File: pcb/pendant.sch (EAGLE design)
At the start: 45 parts, among them CON1 USB_MICROSMT+THRUHULE, Q2 16MHz, SW2 BUTTON_2, T1 SSM3J328R,LF, T2 SSM3J328R,LF, U2 MK20D--VFM5, U3 74LVC1G17DCK, U4 74LVC1G17DCK

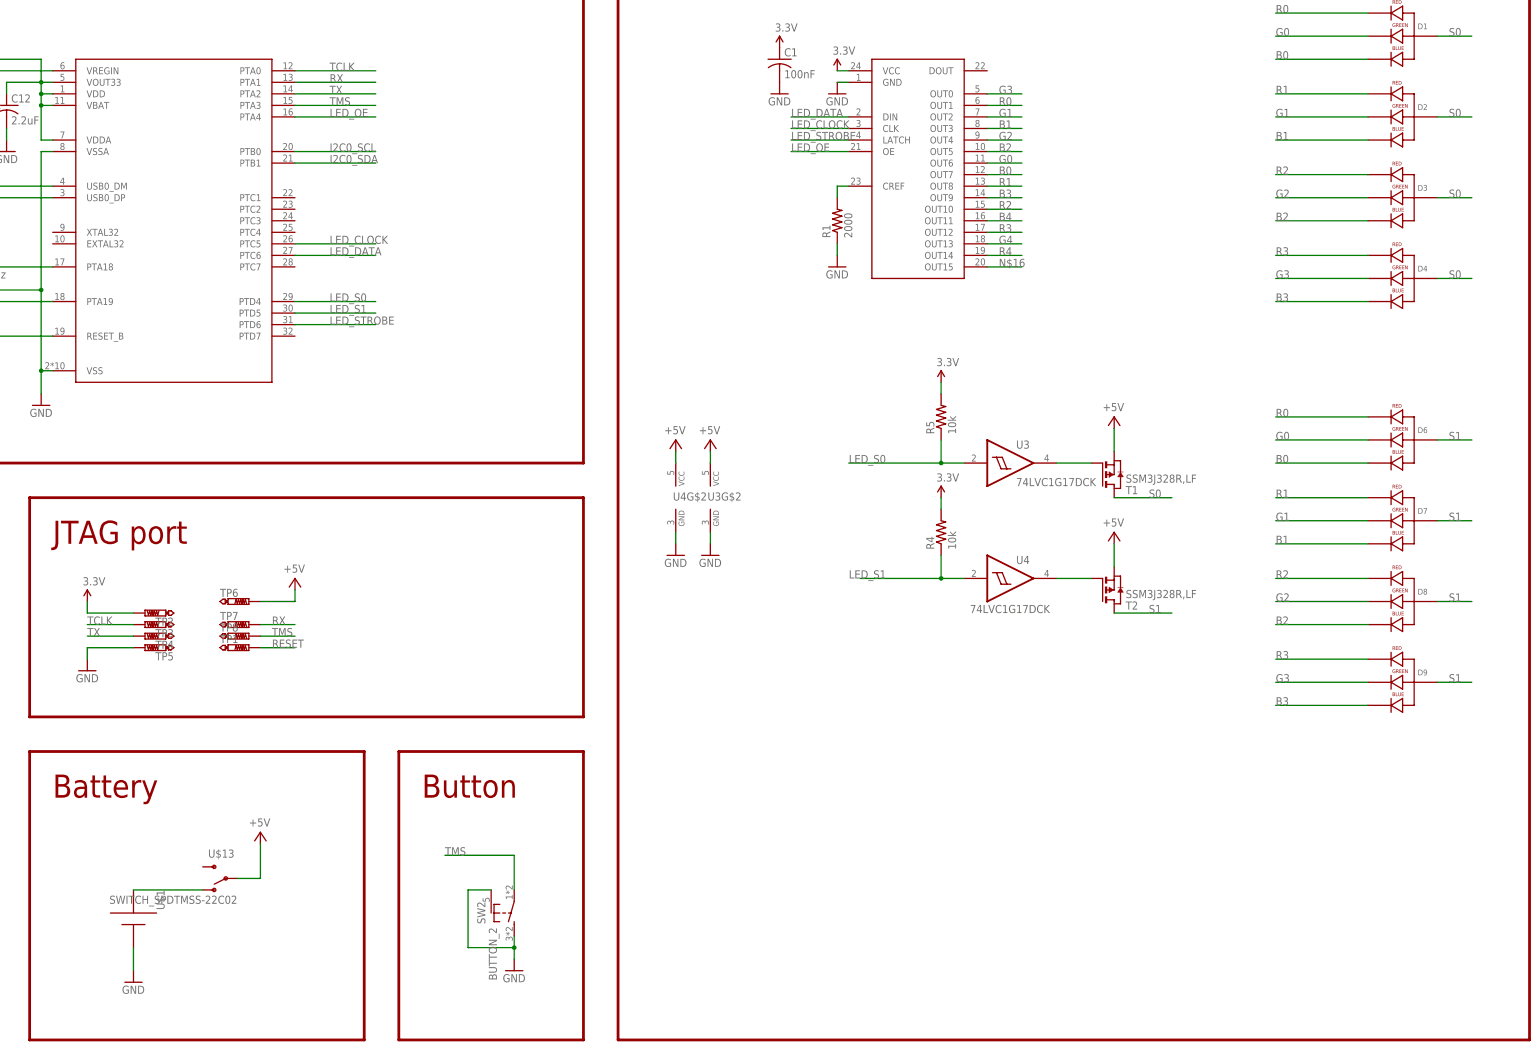
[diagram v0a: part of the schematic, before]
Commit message: fix cap under ICN2026, change led output order, use 5050 LEDs, replace power and tach switches, use 10 LEDs, move test points out from battery
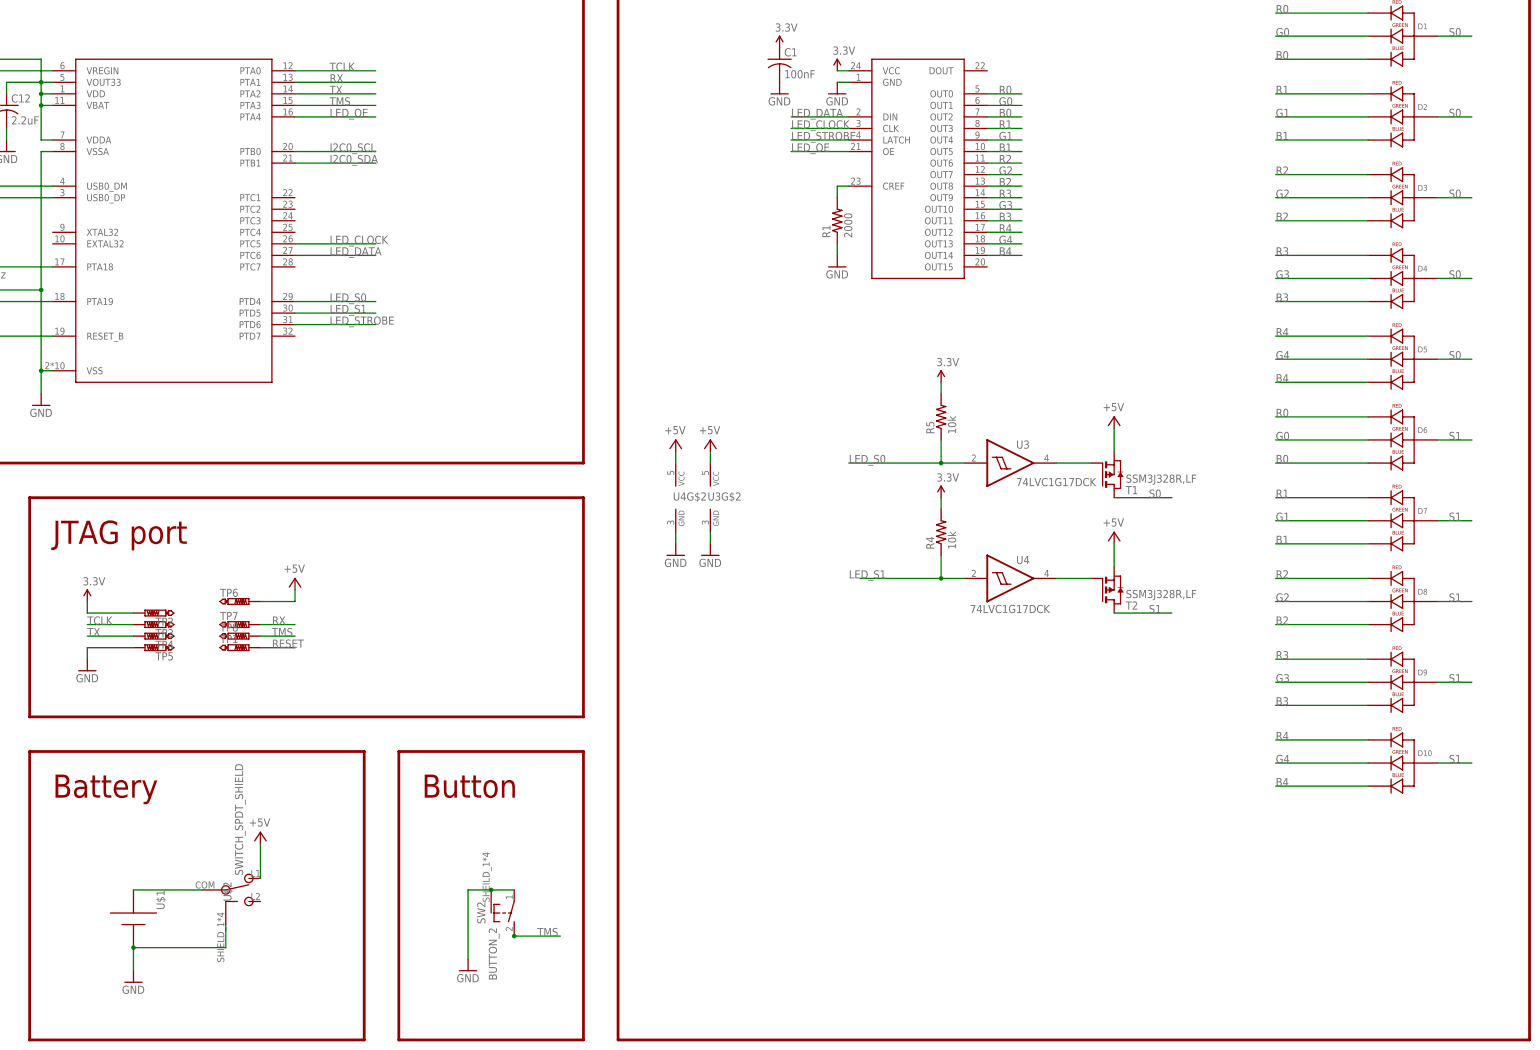
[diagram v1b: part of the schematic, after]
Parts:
- removed U$13: SWITCH_SPDTMSS-22C02, LeoBlinky2014:SWITCH_SPDTMSS-22C02
- added D10, D5: LED-RGB5050, blinkinlabs:LED-RGB5050
- added U$2: SWITCH_SPDT_SHIELD, blinkinlabs:SWITCH_SPDT_SHIELD
- D1, D2, D3, D4, D6, D7, D8, D9: value LED-RGB-CA-THRUCLEAR -> LED-RGB5050; device SparkFun-LED:LED-RGB-CA-THRUCLEAR -> blinkinlabs:LED-RGB5050
- Q2: device blinkinlabs:CRYSTAL_4PAD2520 -> blinkinlabs:CRYSTAL_4PAD
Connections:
- removed net N$16: U$5.OUT15
- net +5V: now also U$2.L1; no longer U$13.P
- net B0: now also U$5.OUT2; no longer U$5.OUT7
- net B1: now also U$5.OUT5; no longer U$5.OUT3
- net B2: now also U$5.OUT8; no longer U$5.OUT5
- net B3: now also U$5.OUT11; no longer U$5.OUT9
- net B4: now also D10.BLUE_CATHODE, D5.BLUE_CATHODE, U$5.OUT14; no longer U$5.OUT11
- net G0: now also U$5.OUT1; no longer U$5.OUT6
- net G1: now also U$5.OUT4; no longer U$5.OUT2
- net G2: now also U$5.OUT7; no longer U$5.OUT4
- net G3: now also U$5.OUT10; no longer U$5.OUT0
- net G4: now also D10.GREEN_CATHODE, D5.GREEN_CATHODE
- net GND: now also SW2.P, U$2.SHIELD; no longer SW2.S
- net N$2: now also U$2.COM; no longer U$13.O
- net R0: now also U$5.OUT0; no longer U$5.OUT1
- net R1: now also U$5.OUT3; no longer U$5.OUT8
- net R2: now also U$5.OUT6; no longer U$5.OUT10
- net R3: now also U$5.OUT9; no longer U$5.OUT12
- net R4: now also D10.RED_CATHODE, D5.RED_CATHODE, U$5.OUT12; no longer U$5.OUT14
- net S0: now also D5.ANODE
- net S1: now also D10.ANODE
- net TMS: now also SW2.S; no longer SW2.P
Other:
- moved on the sheet: SW2

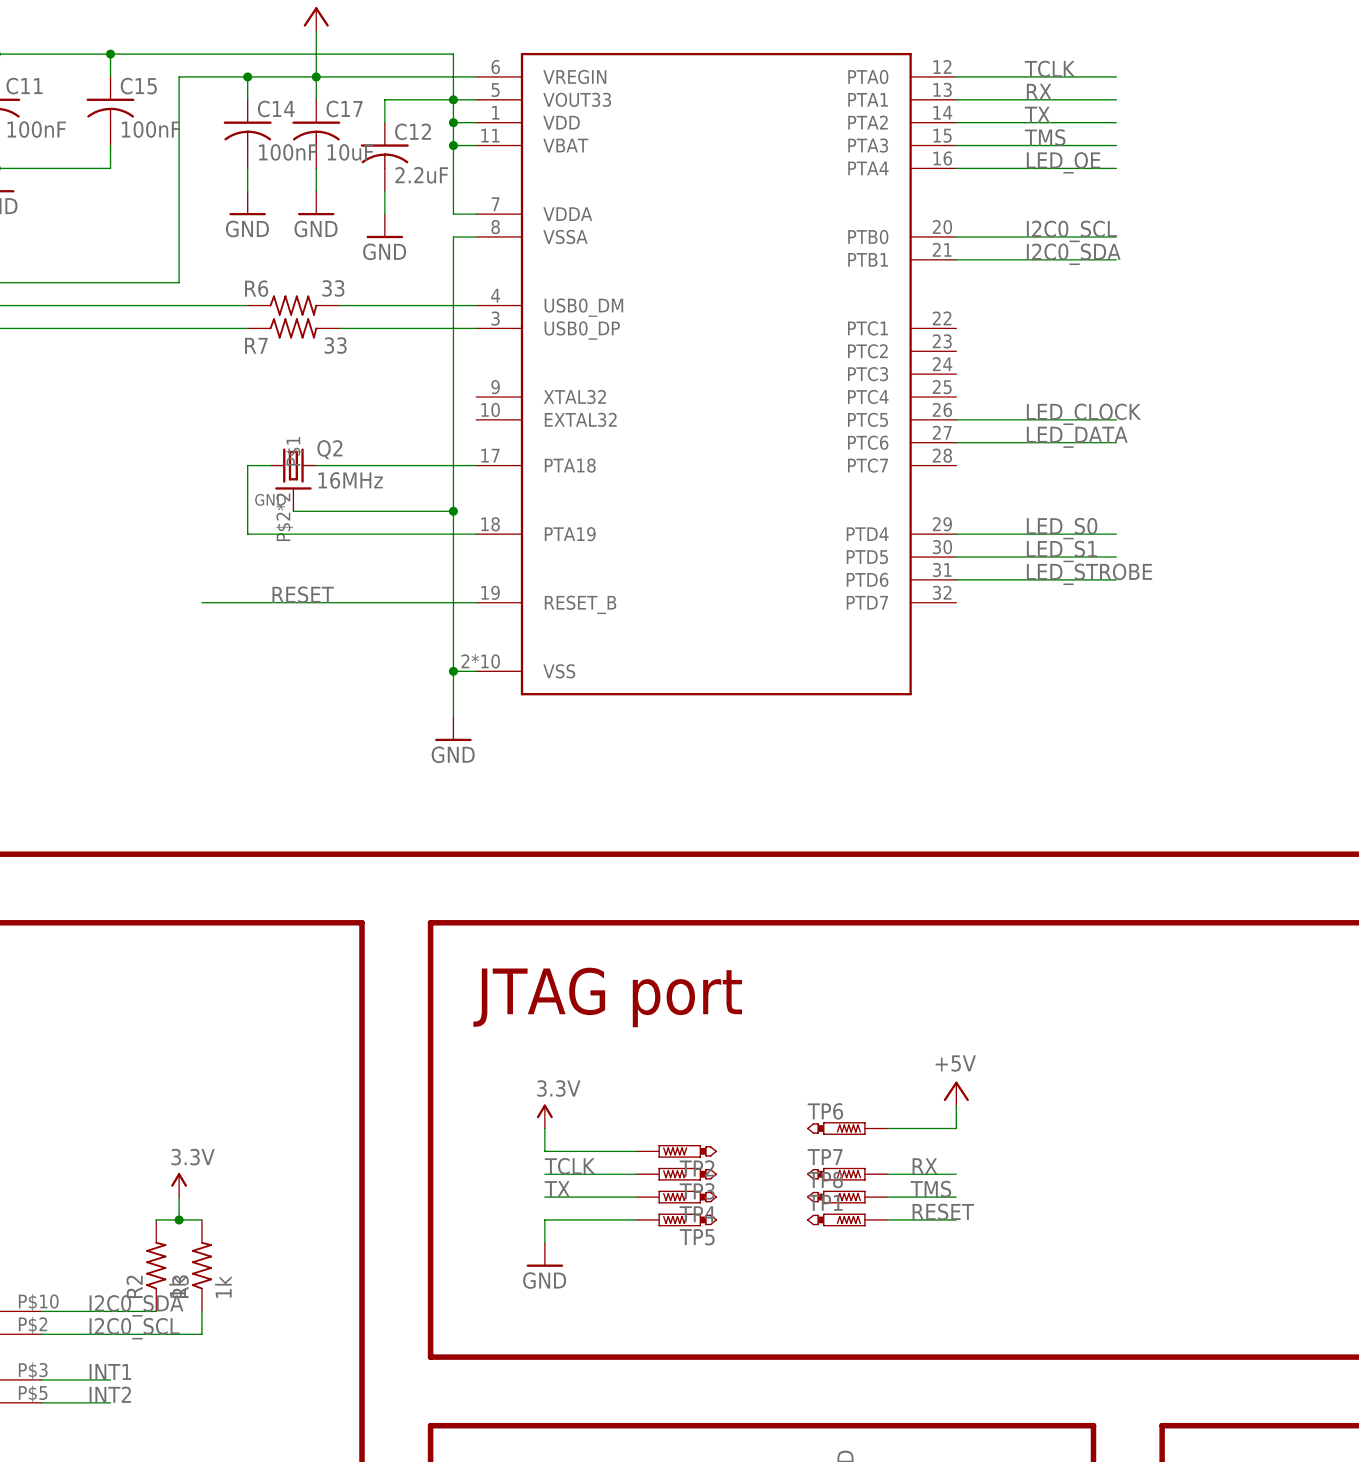
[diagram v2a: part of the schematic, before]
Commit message: Adding support for accelerometer
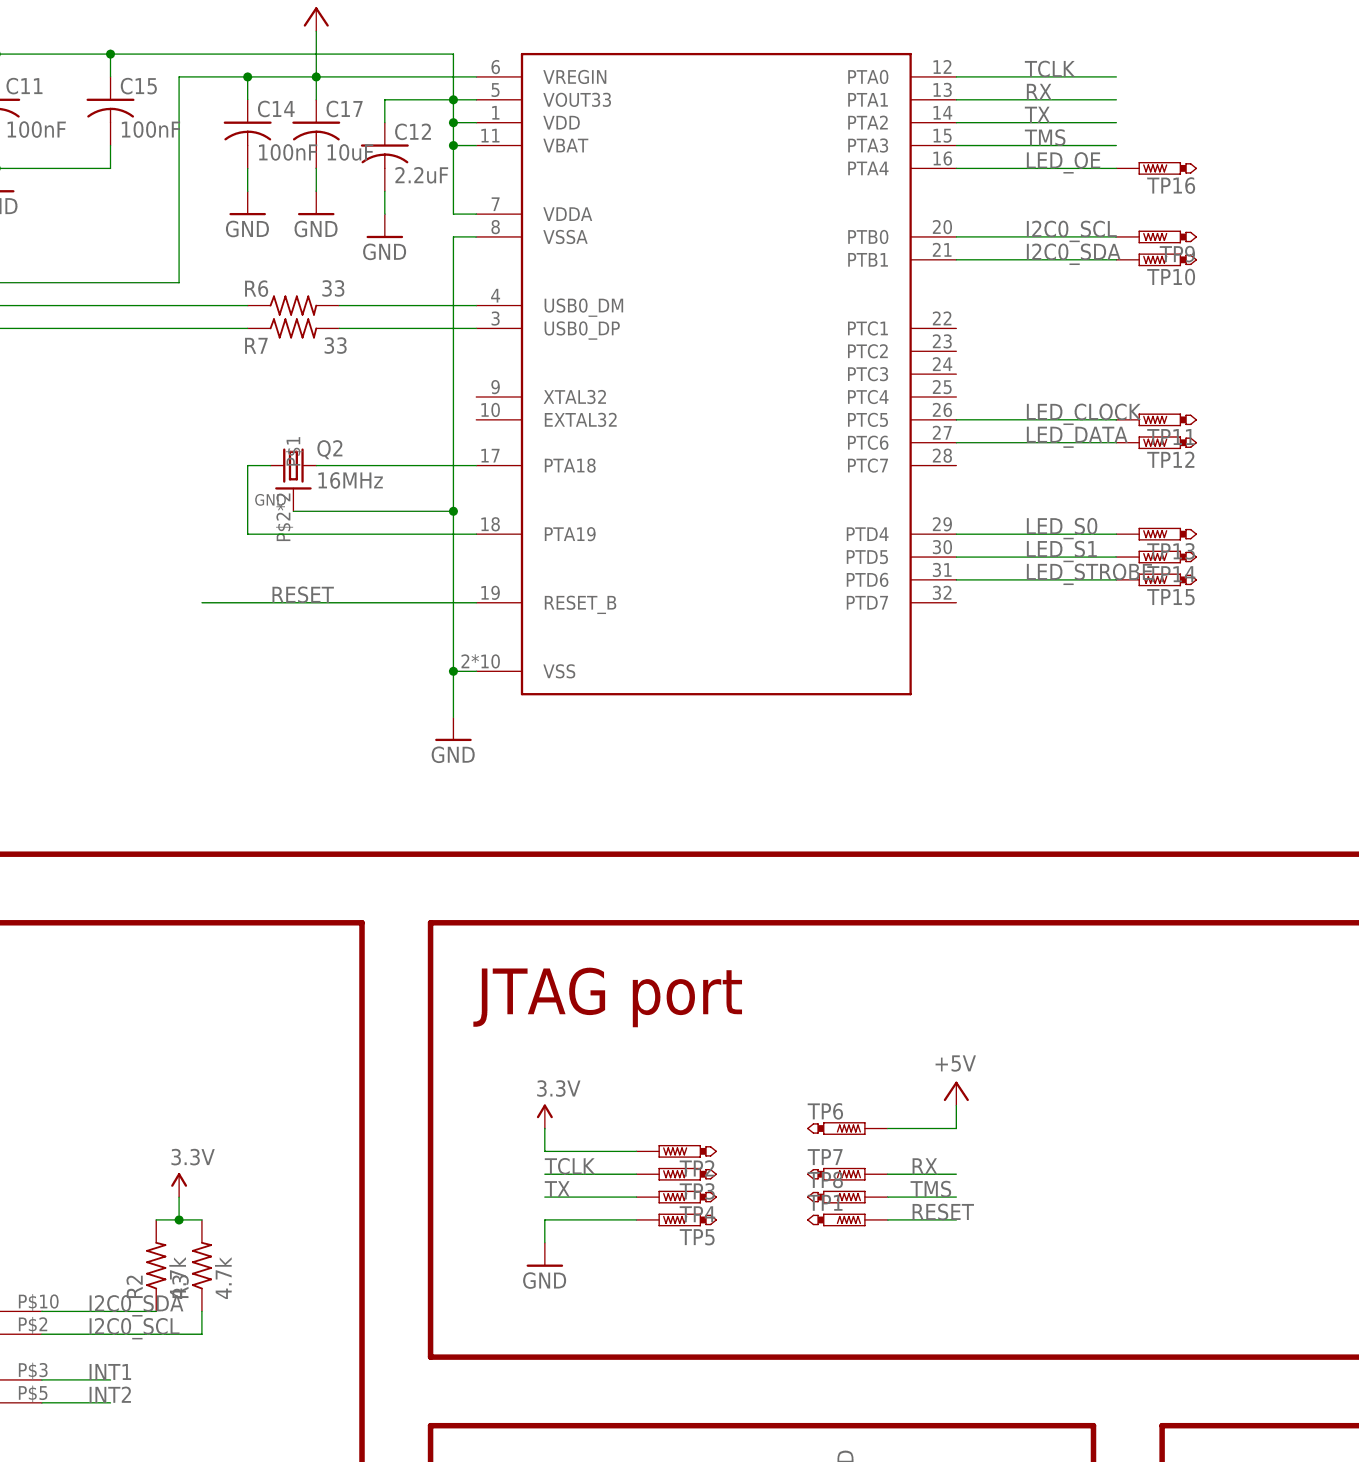
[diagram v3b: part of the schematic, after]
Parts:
- added TP10, TP11, TP12, TP13, TP14, TP15, TP16, TP9: PTR1B1,27, testpad:PTR1B1,27
- R2, R3: value 1k -> 4.7k
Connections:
- net I2C0_SCL: now also TP9.TP
- net I2C0_SDA: now also TP10.TP
- net LED_CLOCK: now also TP11.TP
- net LED_DATA: now also TP12.TP
- net LED_OE: now also TP16.TP
- net LED_S0: now also TP13.TP
- net LED_S1: now also TP14.TP
- net LED_STROBE: now also TP15.TP
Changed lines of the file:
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@@
 <part name="GND5" library="SparkFun-Aesthetics" deviceset="GND" device=""/>
 <part name="SUPPLY6" library="SparkFun-Aesthetics" deviceset="3.3V" device=""/>
-<part name="R2" library="adafruit" deviceset="R-US_" device="R0402" value="1k"/>
-<part name="R3" library="adafruit" deviceset="R-US_" device="R0402" value="1k"/>
+<part name="R2" library="adafruit" deviceset="R-US_" device="R0402" value="4.7k"/>
+<part name="R3" library="adafruit" deviceset="R-US_" device="R0402" value="4.7k"/>
 <part name="SUPPLY7" library="SparkFun-Aesthetics" deviceset="3.3V" device=""/>
 <part name="C2" library="adafruit" deviceset="C-US" device="C0402" value="100nF"/>
@@
 <part name="D10" library="blinkinlabs" deviceset="LED-RGB" device="5050"/>
 <part name="U$2" library="blinkinlabs" deviceset="SWITCH_SPDT_SHIELD" device=""/>
+<part name="TP9" library="testpad" deviceset="PTR1" device="B1,27"/>
+<part name="TP11" library="testpad" deviceset="PTR1" device="B1,27"/>
+<part name="TP12" library="testpad" deviceset="PTR1" device="B1,27"/>
+<part name="TP13" library="testpad" deviceset="PTR1" device="B1,27"/>
+<part name="TP14" library="testpad" deviceset="PTR1" device="B1,27"/>
+<part name="TP15" library="testpad" deviceset="PTR1" device="B1,27"/>
+<part name="TP16" library="testpad" deviceset="PTR1" device="B1,27"/>
+<part name="TP10" library="testpad" deviceset="PTR1" device="B1,27"/>
 </parts>
 <sheets>
@@
 <instance part="D10" gate="G$1" x="439.42" y="193.04"/>
 <instance part="U$2" gate="G$1" x="187.96" y="165.1"/>
+<instance part="TP9" gate="G$1" x="218.44" y="327.66" rot="R90"/>
+<instance part="TP11" gate="G$1" x="218.44" y="307.34" rot="R90"/>
+<instance part="TP12" gate="G$1" x="218.44" y="304.8" rot="R90"/>
+<instance part="TP13" gate="G$1" x="218.44" y="294.64" rot="R90"/>
+<instance part="TP14" gate="G$1" x="218.44" y="292.1" rot="R90"/>
+<instance part="TP15" gate="G$1" x="218.44" y="289.56" rot="R90"/>
+<instance part="TP16" gate="G$1" x="218.44" y="335.28" rot="R90"/>
+<instance part="TP10" gate="G$1" x="218.44" y="325.12" rot="R90"/>
 </instances>
 <busses>
@@
 <wire x1="198.12" y1="335.28" x2="215.9" y2="335.28" width="0.1524" layer="91"/>
 <label x="205.74" y="335.28" size="1.778" layer="95"/>
+<pinref part="TP16" gate="G$1" pin="TP"/>
 </segment>
 </net>
@@
 <wire x1="198.12" y1="327.66" x2="215.9" y2="327.66" width="0.1524" layer="91"/>
 <label x="205.74" y="327.66" size="1.778" layer="95"/>
+<pinref part="TP9" gate="G$1" pin="TP"/>
 </segment>
 </net>
@@
 <wire x1="215.9" y1="325.12" x2="198.12" y2="325.12" width="0.1524" layer="91"/>
 <label x="205.74" y="325.12" size="1.778" layer="95"/>
+<pinref part="TP10" gate="G$1" pin="TP"/>
 </segment>
 </net>
@@
 <wire x1="215.9" y1="304.8" x2="198.12" y2="304.8" width="0.1524" layer="91"/>
 <label x="205.74" y="304.8" size="1.778" layer="95"/>
+<pinref part="TP12" gate="G$1" pin="TP"/>
 </segment>
 </net>
@@
 <wire x1="198.12" y1="307.34" x2="215.9" y2="307.34" width="0.1524" layer="91"/>
 <label x="205.74" y="307.34" size="1.778" layer="95"/>
+<pinref part="TP11" gate="G$1" pin="TP"/>
 </segment>
 </net>
@@
 <wire x1="198.12" y1="289.56" x2="215.9" y2="289.56" width="0.1524" layer="91"/>
 <label x="205.74" y="289.56" size="1.778" layer="95"/>
+<pinref part="TP15" gate="G$1" pin="TP"/>
 </segment>
 </net>
@@
 <wire x1="198.12" y1="294.64" x2="215.9" y2="294.64" width="0.1524" layer="91"/>
 <label x="205.74" y="294.64" size="1.778" layer="95"/>
+<pinref part="TP13" gate="G$1" pin="TP"/>
 </segment>
 <segment>
@@
 <wire x1="198.12" y1="292.1" x2="215.9" y2="292.1" width="0.1524" layer="91"/>
 <label x="205.74" y="292.1" size="1.778" layer="95"/>
-</segment>
-<segment>
+<pinref part="TP14" gate="G$1" pin="TP"/>
+</segment>
+<segment>
